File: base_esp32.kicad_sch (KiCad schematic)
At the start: 77 parts, among them J1 Input Source, J10 H_IO15_OUT, J11 H_IO32_OUT, J12 H_IO02_OUT, J13 H_IO04_OUT, J14 H_5V, J15 S_5V, J16 H_3V3_1, J17 H_IO34, J18 H_IO35, J19 H_IO36, J2 BYPASS SRC 5V, J20 H_IO39, J21 S_3V3_1, J22 H_3V3_2, J23 H_KEYPAD, J24 H_I2C, J25 H_SPI, J26 TX_RX, J27 S_3V3_2, J28 H_GND, J29 S_KEYPAD, J3 BYPASS SRC 3V3, J30 S_I2C, J31 S_SPI, J32 S_GND, J33 H_Src Board, J4 H_IO33, J5 H_IO15, J6 H_IO32, J7 H_IO02, J8 H_IO04, J9 H_IO33_OUT, SW1 INPUT_D1, SW2 INPUT_D2, SW3 SW_DIP_INPUTS, SW4 ENABLE, SW5 SW_DIP_KEYPAD, SW6 Selector Input 1, SW7 Selector Input 2, SW8 BOOT, U1 LM7805_TO220, U2 AMS1117, U3 AMS1117, U4 ESP32-DevKitC

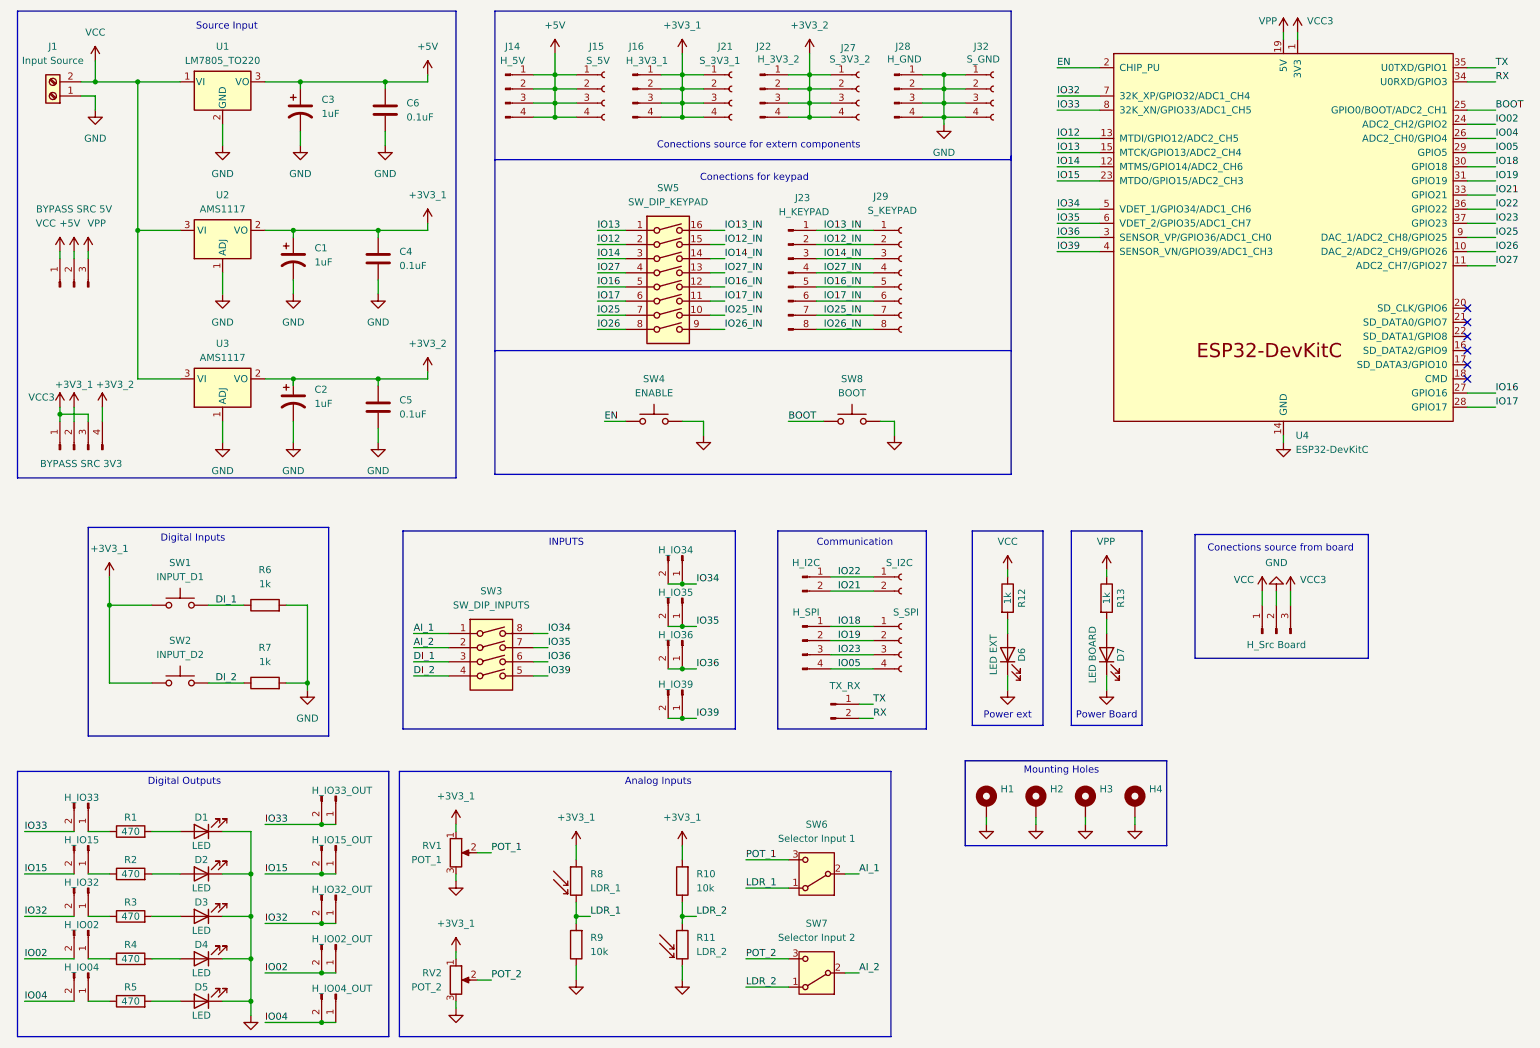
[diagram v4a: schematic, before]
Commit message: add: some components to schematic
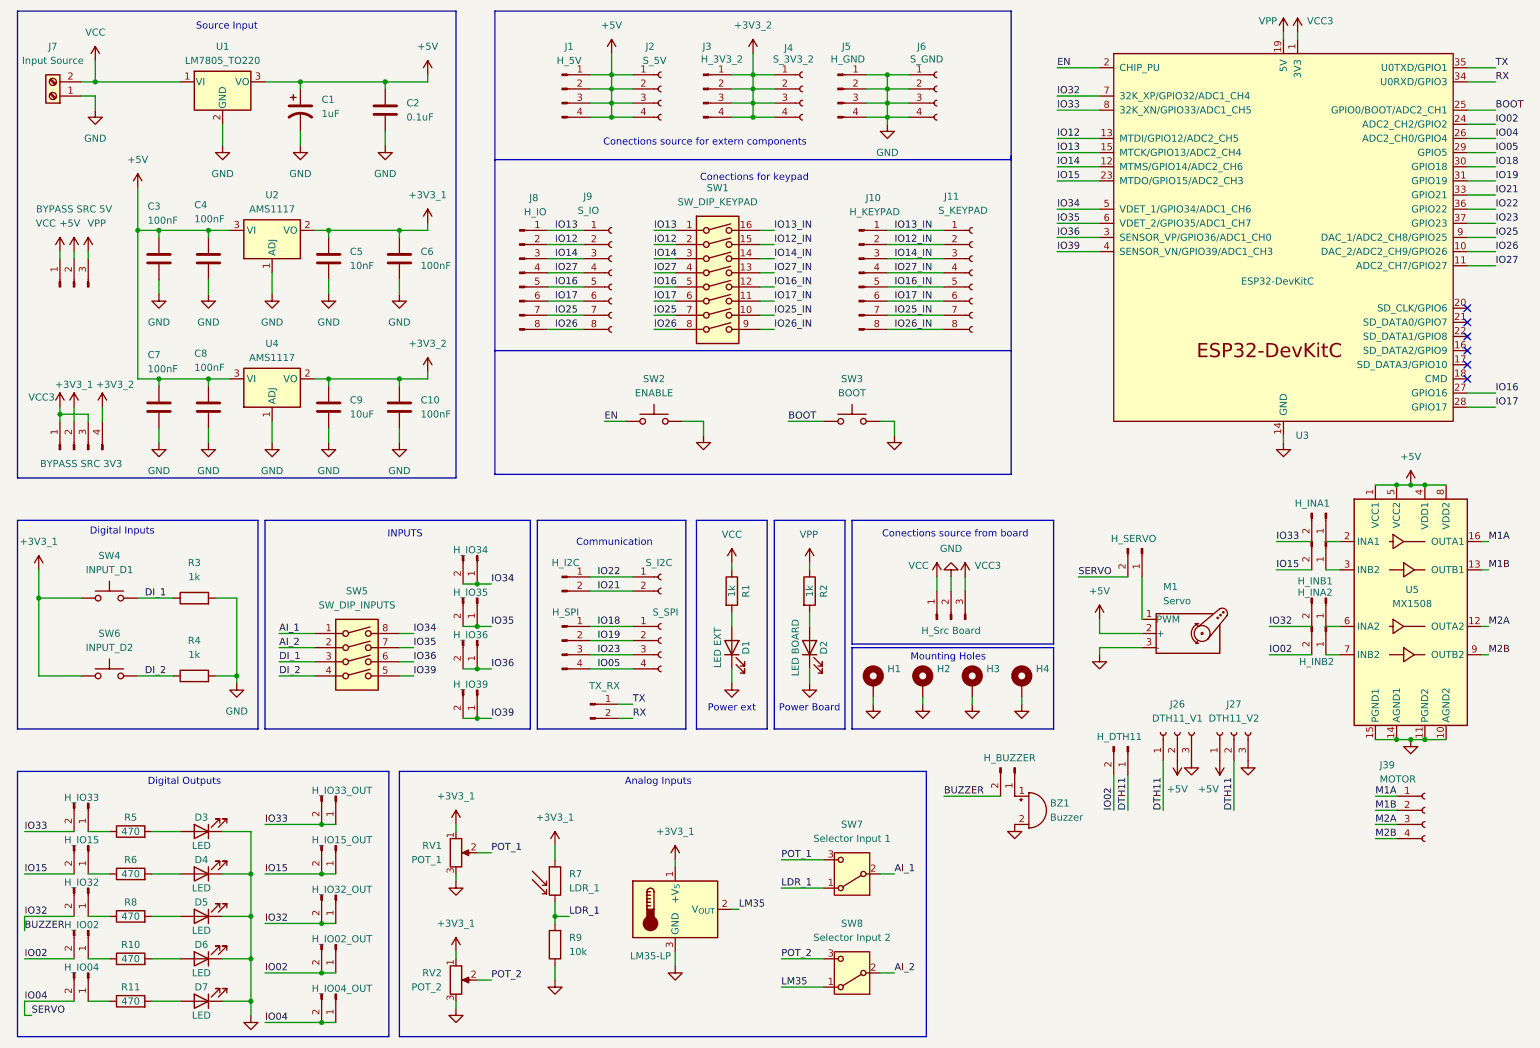
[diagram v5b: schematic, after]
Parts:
- removed C1, C2: 1uF, Capacitor_THT:CP_Radial_D5.0mm_P2.50mm, symbol Device:C_Polarized_US
- removed J16: H_3V3_1, Connector_PinHeader_2.54mm:PinHeader_1x04_P2.54mm_Vertical, symbol Connector:Conn_01x04_Pin
- removed J21: S_3V3_1, Connector_PinSocket_2.54mm:PinSocket_1x04_P2.54mm_Vertical, symbol Connector:Conn_01x04_Socket
- removed R10: 10k, Resistor_THT:R_Axial_DIN0207_L6.3mm_D2.5mm_P10.16mm_Horizontal, symbol Device:R
- removed R11: LDR_2, OptoDevice:R_LDR_5.0x4.1mm_P3mm_Vertical, symbol Sensor_Optical:A9013
- added BZ1: Buzzer, Buzzer_Beeper:MagneticBuzzer_ProSignal_ABI-010-RC, symbol Device:Buzzer
- added C3, C4, C7, C8: 100nF, Capacitor_SMD:C_0805_2012Metric, symbol Device:C
- added C5: 10nF, Capacitor_SMD:C_0805_2012Metric, symbol Device:C
- added C9: 10uF, Capacitor_SMD:C_0805_2012Metric, symbol Device:C
- added J15: H_SERVO, Connector_PinHeader_2.54mm:PinHeader_1x02_P2.54mm_Vertical, symbol Connector:Conn_01x02_Pin
- added J25: H_BUZZER, Connector_PinHeader_2.54mm:PinHeader_1x02_P2.54mm_Vertical, symbol Connector:Conn_01x02_Pin
- added J26: DTH11_V1, Connector_PinSocket_2.54mm:PinSocket_1x03_P2.54mm_Vertical, symbol Connector:Conn_01x03_Socket
- added J27: DTH11_V2, Connector_PinSocket_2.54mm:PinSocket_1x03_P2.54mm_Vertical, symbol Connector:Conn_01x03_Socket
- added J28: H_DTH11, Connector_PinHeader_2.54mm:PinHeader_1x02_P2.54mm_Vertical, symbol Connector:Conn_01x02_Pin
- added J39: MOTOR, Connector_PinSocket_2.54mm:PinSocket_1x04_P2.54mm_Vertical, symbol Connector:Conn_01x04_Socket
- added J40: H_INA1, Connector_PinHeader_2.54mm:PinHeader_1x02_P2.54mm_Vertical, symbol Connector:Conn_01x02_Pin
- added J41: H_INB1, Connector_PinHeader_2.54mm:PinHeader_1x02_P2.54mm_Vertical, symbol Connector:Conn_01x02_Pin
- added J42: H_INA2, Connector_PinHeader_2.54mm:PinHeader_1x02_P2.54mm_Vertical, symbol Connector:Conn_01x02_Pin
- added J43: H_INB2, Connector_PinHeader_2.54mm:PinHeader_1x02_P2.54mm_Vertical, symbol Connector:Conn_01x02_Pin
- added J8: H_IO, Connector_PinHeader_2.54mm:PinHeader_1x08_P2.54mm_Vertical, symbol Connector:Conn_01x08_Pin
- added J9: S_IO, Connector_PinSocket_2.54mm:PinSocket_1x08_P2.54mm_Vertical, symbol Connector:Conn_01x08_Socket
- added M1: Servo, Connector_PinHeader_2.54mm:PinHeader_1x03_P2.54mm_Vertical, symbol Motor:Motor_Servo_Futaba_J
- added U5: MX1508, Package_SO:SOP-16_3.9x9.9mm_P1.27mm, symbol MX1508:MX1508
- added U6: LM35-LP, Package_TO_SOT_THT:TO-92_Inline, symbol Sensor_Temperature:LM35-LP
- C10: renamed from C5; value 0.1uF -> 100nF; footprint Capacitor_THT:C_Disc_D5.0mm_W2.5mm_P5.00mm -> Capacitor_SMD:C_0805_2012Metric
- C6: renamed from C4; value 0.1uF -> 100nF; footprint Capacitor_THT:C_Disc_D5.0mm_W2.5mm_P5.00mm -> Capacitor_SMD:C_0805_2012Metric
- D1: renamed from D6; footprint LED_THT:LED_D3.0mm -> LED_SMD:LED_0805_2012Metric
- D2: renamed from D7; footprint LED_THT:LED_D3.0mm -> LED_SMD:LED_0805_2012Metric
- R1: renamed from R12; footprint Resistor_THT:R_Axial_DIN0207_L6.3mm_D2.5mm_P10.16mm_Horizontal -> Resistor_SMD:R_0805_2012Metric_Pad1.20x1.40mm_HandSolder
- R2: renamed from R13; footprint Resistor_THT:R_Axial_DIN0207_L6.3mm_D2.5mm_P10.16mm_Horizontal -> Resistor_SMD:R_0805_2012Metric_Pad1.20x1.40mm_HandSolder
- renumbered C3 to C1, C6 to C2, D1 to D3, D2 to D4, D3 to D5, D4 to D6, D5 to D7, J14 to J1, J23 to J10, J29 to J11, J2 to J12, J3 to J13, J17 to J14, J33 to J16, J24 to J17, J30 to J18, J18 to J19, J15 to J2, J19 to J20, J25 to J21, J31 to J22, J20 to J23, J26 to J24, J9 to J29, J22 to J3, J4 to J30, J5 to J31, J10 to J32, J6 to J33, J11 to J34, J7 to J35, J12 to J36, J8 to J37, J13 to J38, J27 to J4, J28 to J5, J32 to J6, J1 to J7, R4 to R10, R5 to R11, R6 to R3, R7 to R4, R1 to R5, R2 to R6, R8 to R7, R3 to R8, SW5 to SW1, SW4 to SW2, SW8 to SW3, SW1 to SW4, SW3 to SW5, SW2 to SW6, SW6 to SW7, SW7 to SW8, U4 to U3, U3 to U4
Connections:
- net +3V3_1: now also C5.1, U6.1 (+V_{S})
- net +3V3_2: now also C9.1
- net +5V: now also U2.3 (VI), U4.3 (VI), C3.1, C4.1, C7.1, C8.1, J26.2 (Pin_2), J27.1 (Pin_1), M1.2 (+), U5.1 (VCC1), U5.4 (VDD1), U5.5 (VCC2), U5.8 (VDD2)
- net GND: now also BZ1.2 (-), C3.2, C4.2, C5.2, C7.2, C8.2, C9.2, J26.3 (Pin_3), J27.3 (Pin_3), M1.3 (-), U5.10 (AGND2), U5.11 (PGND2), U5.14 (AGND1), U5.15 (PGND1), U6.3 (GND)
- net IO02: now also J28.2 (Pin_2), J43.2 (Pin_2)
- net IO04: now also J15.2 (Pin_2)
- net IO12: now also J8.2 (Pin_2), J9.2 (Pin_2)
- net IO13: now also J8.1 (Pin_1), J9.1 (Pin_1)
- net IO14: now also J8.3 (Pin_3), J9.3 (Pin_3)
- net IO15: now also J41.2 (Pin_2)
- net IO16: now also J8.5 (Pin_5), J9.5 (Pin_5)
- net IO17: now also J8.6 (Pin_6), J9.6 (Pin_6)
- net IO25: now also J8.7 (Pin_7), J9.7 (Pin_7)
- net IO26: now also J8.8 (Pin_8), J9.8 (Pin_8)
- net IO27: now also J8.4 (Pin_4), J9.4 (Pin_4)
- net IO33: now also J40.2 (Pin_2)
- net VCC: no longer U2.3 (VI), U4.3 (VI)
- net IO32 renamed BUZZER
- net BUZZER: now also J25.2 (Pin_2), J42.2 (Pin_2)
- net LDR_2 renamed LM35
- net LM35: now also U6.2 (V_{OUT})
- new net: J40.1 (Pin_1), U5.2 (INA1)
- new net: J15.1 (Pin_1), M1.1 (PWM)
- new net: J42.1 (Pin_1), U5.6 (INA2)
- new net: J41.1 (Pin_1), U5.3 (INB2)
- new net: J43.1 (Pin_1), U5.7 (INB2)
- new net: BZ1.1 (+), J25.1 (Pin_1)
- new net DTH11: J26.1 (Pin_1), J27.2 (Pin_2), J28.1 (Pin_1)
- new net M1A: J39.1 (Pin_1), U5.16 (OUTA1)
- new net M1B: J39.2 (Pin_2), U5.13 (OUTB1)
- new net M2A: J39.3 (Pin_3), U5.12 (OUTA2)
- new net M2B: J39.4 (Pin_4), U5.9 (OUTB2)
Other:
- moved on the sheet: C10, C6, D1, D2, H1, H2, H3, H4, J1, J10, J11, J2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

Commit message: rm: header
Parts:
- removed SW1: SW_DIP_KEYPAD, Button_Switch_THT:SW_DIP_SPSTx08_Slide_9.78x22.5mm_W7.62mm_P2.54mm, symbol Switch:SW_DIP_x08
- added SW1: SW_DIP_KEYPAD_1, Button_Switch_THT:SW_DIP_SPSTx04_Slide_9.78x12.34mm_W7.62mm_P2.54mm, symbol Switch:SW_DIP_x04
- added SW2: SW_DIP_KEYPAD_2, Button_Switch_THT:SW_DIP_SPSTx04_Slide_9.78x12.34mm_W7.62mm_P2.54mm, symbol Switch:SW_DIP_x04
- J1: renamed from J16; value H_Src Board -> H_Src_raw
- renumbered J9 to J10, J10 to J11, J11 to J12, J12 to J13, J13 to J14, J40 to J15, J25 to J16, J41 to J17, J15 to J18, J14 to J19, J1 to J2, J17 to J20, J18 to J21, J19 to J22, J42 to J23, J43 to J24, J20 to J25, J21 to J26, J22 to J27, J26 to J28, J27 to J29, J2 to J3, J28 to J30, J23 to J31, J24 to J32, J39 to J33, J29 to J34, J30 to J35, J31 to J36, J32 to J37, J33 to J38, J34 to J39, J3 to J4, J35 to J40, J36 to J41, J37 to J42, J38 to J43, J4 to J5, J5 to J6, J6 to J7, J7 to J8, J8 to J9, SW2 to SW3, SW3 to SW4, SW4 to SW5, SW5 to SW6, SW6 to SW7, SW7 to SW8, SW8 to SW9
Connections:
- net GND: no longer J1.2 (Pin_2)
- net IO12: now also SW1.2
- net IO12_IN: now also SW1.7
- net IO13: now also SW1.1
- net IO13_IN: now also SW1.8
- net IO14: now also SW1.3
- net IO14_IN: now also SW1.6
- net IO16: now also SW2.1
- net IO16_IN: now also SW2.8
- net IO17: now also SW2.2
- net IO17_IN: now also SW2.7
- net IO25: now also SW2.3
- net IO25_IN: now also SW2.6
- net IO26: now also SW2.4
- net IO26_IN: now also SW2.5
- net IO27: now also SW1.4
- net IO27_IN: now also SW1.5
- net VCC: now also J1.2 (Pin_2), J1.3 (Pin_3)
- net VCC3: no longer J1.3 (Pin_3)
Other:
- note removed: "Conections source from board"
- moved on the sheet: BZ1, H1, H2, H3, H4, J28, J29, J33, SW3, SW4

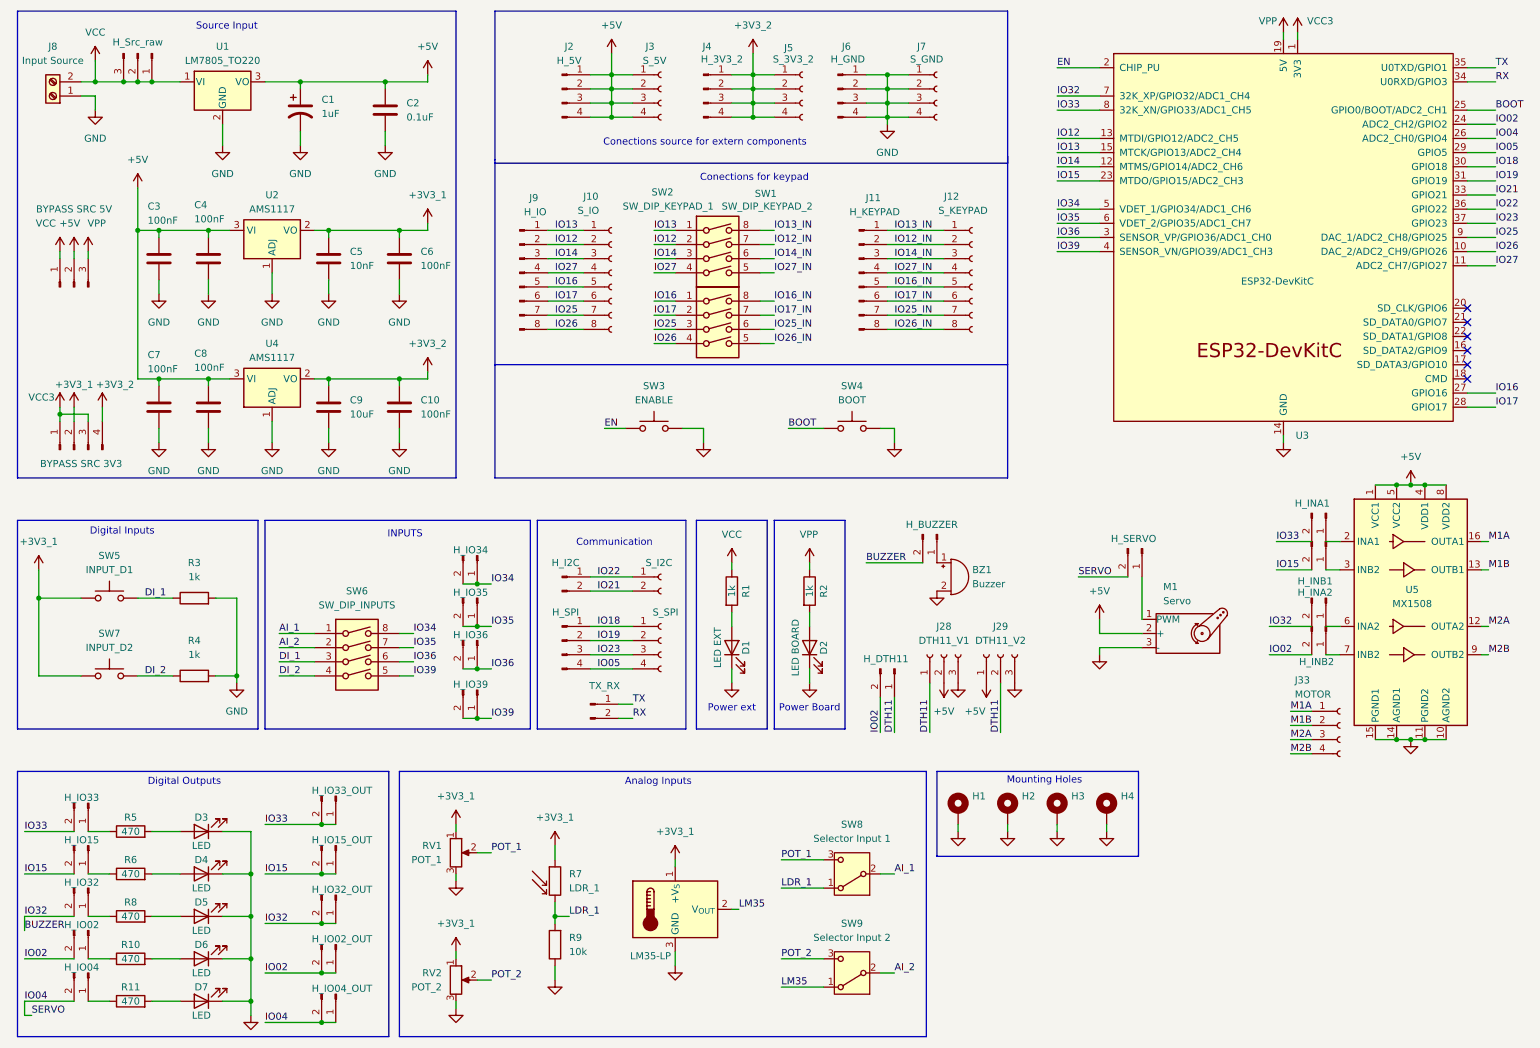
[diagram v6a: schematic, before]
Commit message: add: ultrasonic
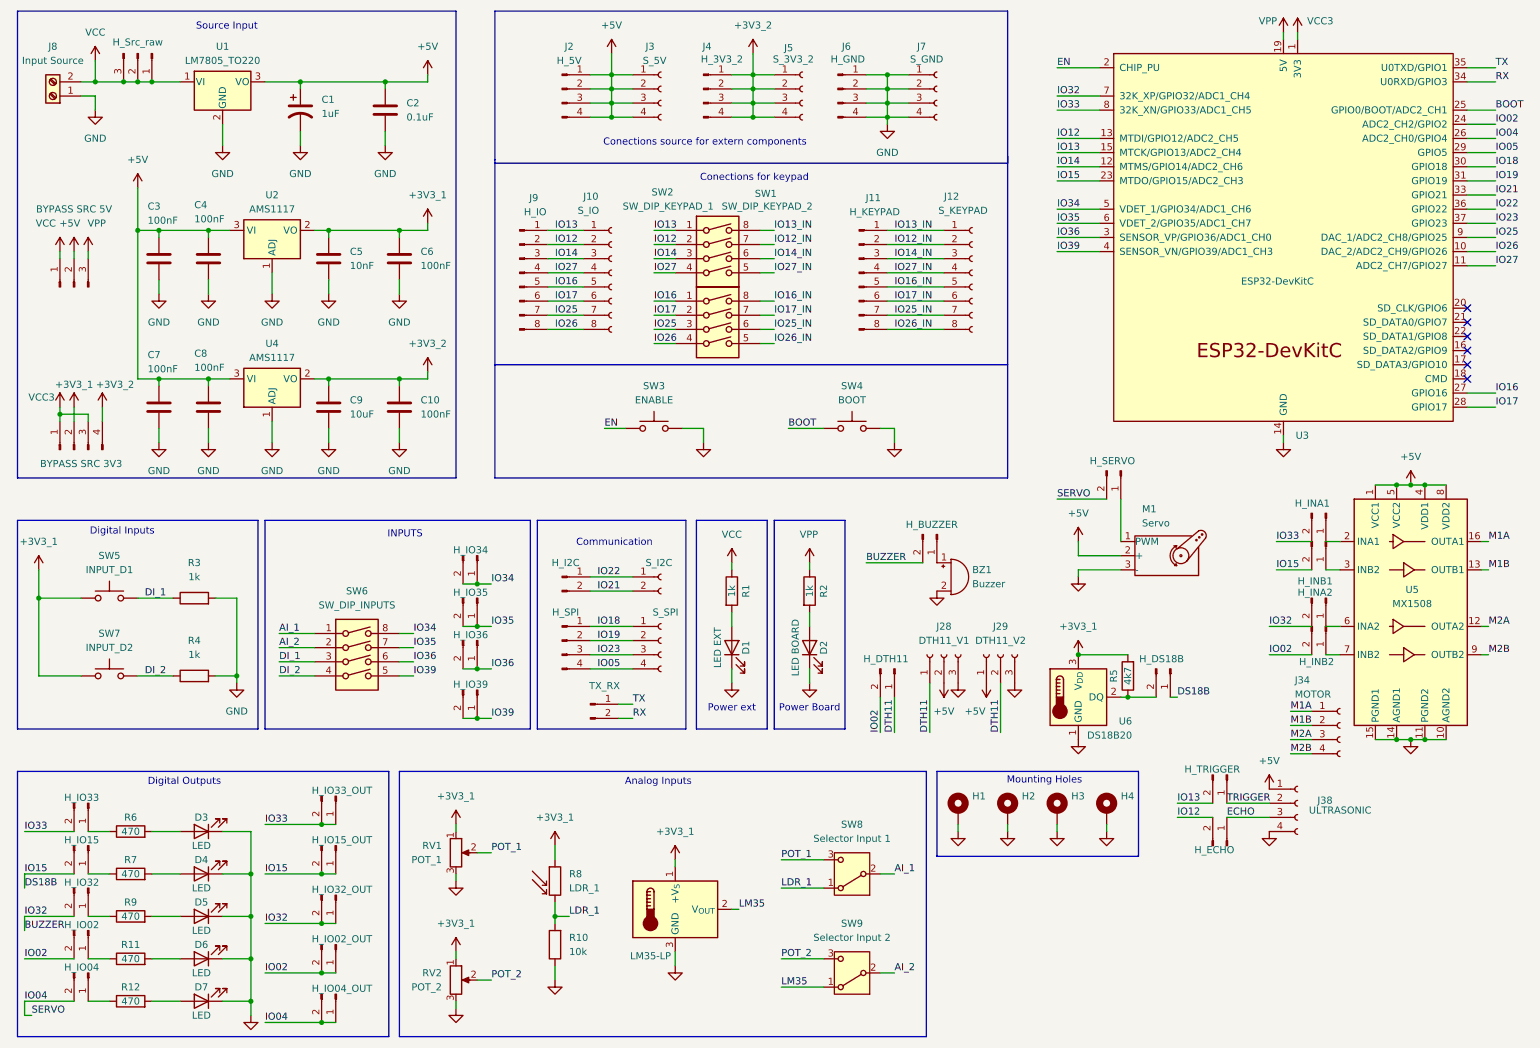
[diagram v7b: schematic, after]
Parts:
- added J31: H_DS18B, Connector_PinHeader_2.54mm:PinHeader_1x02_P2.54mm_Vertical, symbol Connector:Conn_01x02_Pin
- added J35: H_TRIGGER, Connector_PinHeader_2.54mm:PinHeader_1x02_P2.54mm_Vertical, symbol Connector:Conn_01x02_Pin
- added J38: ULTRASONIC, Connector_PinSocket_2.54mm:PinSocket_1x04_P2.54mm_Vertical, symbol Connector:Conn_01x04_Socket
- added J41: H_ECHO, Connector_PinHeader_2.54mm:PinHeader_1x02_P2.54mm_Vertical, symbol Connector:Conn_01x02_Pin
- added R5: 4k7, Resistor_THT:R_Axial_DIN0207_L6.3mm_D2.5mm_P10.16mm_Horizontal, symbol Device:R
- added U6: DS18B20, Package_TO_SOT_THT:TO-92_Inline, symbol Sensor_Temperature:DS18B20
- renumbered J18 to J15, J15 to J16, J16 to J17, J17 to J18, J31 to J32, J32 to J33, J33 to J34, J34 to J36, J35 to J37, J36 to J39, J37 to J40, J38 to J42, J39 to J43, J40 to J44, J41 to J45, J42 to J46, J43 to J47, R9 to R10, R10 to R11, R11 to R12, R5 to R6, R6 to R7, R7 to R8, R8 to R9, U6 to U7
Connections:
- net +3V3_1: now also R5.2, U6.3 (V_{DD})
- net +5V: now also J38.1 (Pin_1)
- net GND: now also J38.4 (Pin_4), U6.1 (GND)
- net IO12: now also J41.2 (Pin_2)
- net IO13: now also J35.2 (Pin_2)
- net IO15 renamed DS18B
- net DS18B: now also J31.1 (Pin_1)
- new net: J31.2 (Pin_2), R5.1, U6.2 (DQ)
- new net ECHO: J38.3 (Pin_3), J41.1 (Pin_1)
- new net TRIGGER: J35.1 (Pin_1), J38.2 (Pin_2)
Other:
- moved on the sheet: M1

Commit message: add: router
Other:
- moved on the sheet: J34
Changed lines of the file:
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@@
 	(wire
 		(pts
-			(xy 241.3 138.43) (xy 245.11 138.43)
+			(xy 241.3 134.62) (xy 245.11 134.62)
 		)
 		(stroke
@@
 	(wire
 		(pts
-			(xy 241.3 146.05) (xy 245.11 146.05)
+			(xy 241.3 142.24) (xy 245.11 142.24)
 		)
 		(stroke
@@
 	(wire
 		(pts
-			(xy 241.3 143.51) (xy 245.11 143.51)
+			(xy 241.3 139.7) (xy 245.11 139.7)
 		)
 		(stroke
@@
 	(wire
 		(pts
-			(xy 241.3 140.97) (xy 245.11 140.97)
+			(xy 241.3 137.16) (xy 245.11 137.16)
 		)
 		(stroke
@@
 	)
 	(label "M1A"
-		(at 241.3 138.43 0)
+		(at 241.3 134.62 0)
 		(fields_autoplaced yes)
 		(effects
@@
 	)
 	(label "M1B"
-		(at 241.3 140.97 0)
+		(at 241.3 137.16 0)
 		(fields_autoplaced yes)
 		(effects
@@
 	)
 	(label "M2B"
-		(at 241.3 146.05 0)
+		(at 241.3 142.24 0)
 		(fields_autoplaced yes)
 		(effects
@@
 	)
 	(label "M2A"
-		(at 241.3 143.51 0)
+		(at 241.3 139.7 0)
 		(fields_autoplaced yes)
 		(effects
@@
 		(on_board yes)
 		(dnp no)
-		(fields_autoplaced yes)
 		(property "Reference" "#PWR051"
 			(at 237.49 156.21 0)
@@
 		)
 		(property "Value" "+5V"
-			(at 237.49 147.32 0)
+			(at 237.49 148.336 0)
 			(effects
 				(font
@@
 	(symbol
 		(lib_id "Connector:Conn_01x04_Socket")
-		(at 250.19 140.97 0)
+		(at 250.19 137.16 0)
 		(unit 1)
 		(exclude_from_sim no)
@@
 		(dnp no)
 		(property "Reference" "J34"
-			(at 242.062 132.842 0)
+			(at 234.188 136.144 0)
 			(effects
 				(font
@@
 		)
 		(property "Value" "MOTOR"
-			(at 242.062 135.382 0)
+			(at 234.188 138.684 0)
 			(effects
 				(font
@@
 		)
 		(property "Footprint" "Connector_PinSocket_2.54mm:PinSocket_1x04_P2.54mm_Vertical"
-			(at 250.19 140.97 0)
+			(at 250.19 137.16 0)
 			(effects
 				(font
@@
 		)
 		(property "Datasheet" "~"
-			(at 250.19 140.97 0)
+			(at 250.19 137.16 0)
 			(effects
 				(font
@@
 		)
 		(property "Description" "Generic connector, single row, 01x04, script generated"
-			(at 250.19 140.97 0)
+			(at 250.19 137.16 0)
 			(effects
 				(font
